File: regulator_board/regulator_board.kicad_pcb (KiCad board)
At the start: 2 copper layers, 68 parts, among them J1 BATT, J10 5VOUT, J11 9VOUT, J12 9VOUT, J13 9VOUT, J2 5VOUT, J3 5VOUT, J4 5VOUT, J5 5VOUT, J6 5VOUT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

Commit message: regulator design preliminary
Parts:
- moved U3 141.8 mm to (122.9, 82.2)
- moved J13 138.7 mm to (163.8, 123.2), turned to 90 degrees
- moved D3 124.8 mm to (112.5, 90.3)
- moved U2 119.9 mm to (117.8, 86.6)
- moved C14 119.8 mm to (122.5, 88.2)
- moved R5 118.7 mm to (131.2, 84.7)
- moved D5 118.0 mm to (107.3, 97.3)
- moved R4 117.2 mm to (140.7, 81.2)
- moved C6 115.2 mm to (125.5, 90.7)
- moved C13 115.1 mm to (129.9, 93.2)
- moved L2 111.3 mm to (100.1, 84.5)
- moved C7 111.2 mm to (116.0, 100.3)
- moved C10 110.5 mm to (136.3, 81.2)
- moved R13 109.8 mm to (135.6, 84.7)
- moved J11 106.4 mm to (148.6, 123.2), turned to 90 degrees
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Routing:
- net +BATT: track 0.00 -> 13.6 mm
- net Net-(JP1-Pad2): track 0.00 -> 6.28 mm
- net /5V_1: track 0.00 -> 4.02 mm
- net GND: track 0.00 -> 1.19 mm, vias 0 -> 11
- added copper zone on F.Cu, net +BATT
- added copper zone on F.Cu, net /5V_1
- added copper zone on B.Cu, net GND
- added copper zone on F.Cu, net GND
- added copper zone on F.Cu, net Net-(C2-Pad1)
- added copper zone on F.Cu, net Net-(C2-Pad2)
- added copper zone on F.Cu, net Net-(C3-Pad2)
- added copper zone on F.Cu, net Net-(F1-Pad1)
- added copper zone on F.Cu, net Net-(F2-Pad2)
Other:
- board outline added: 110.7 x 36.6 mm

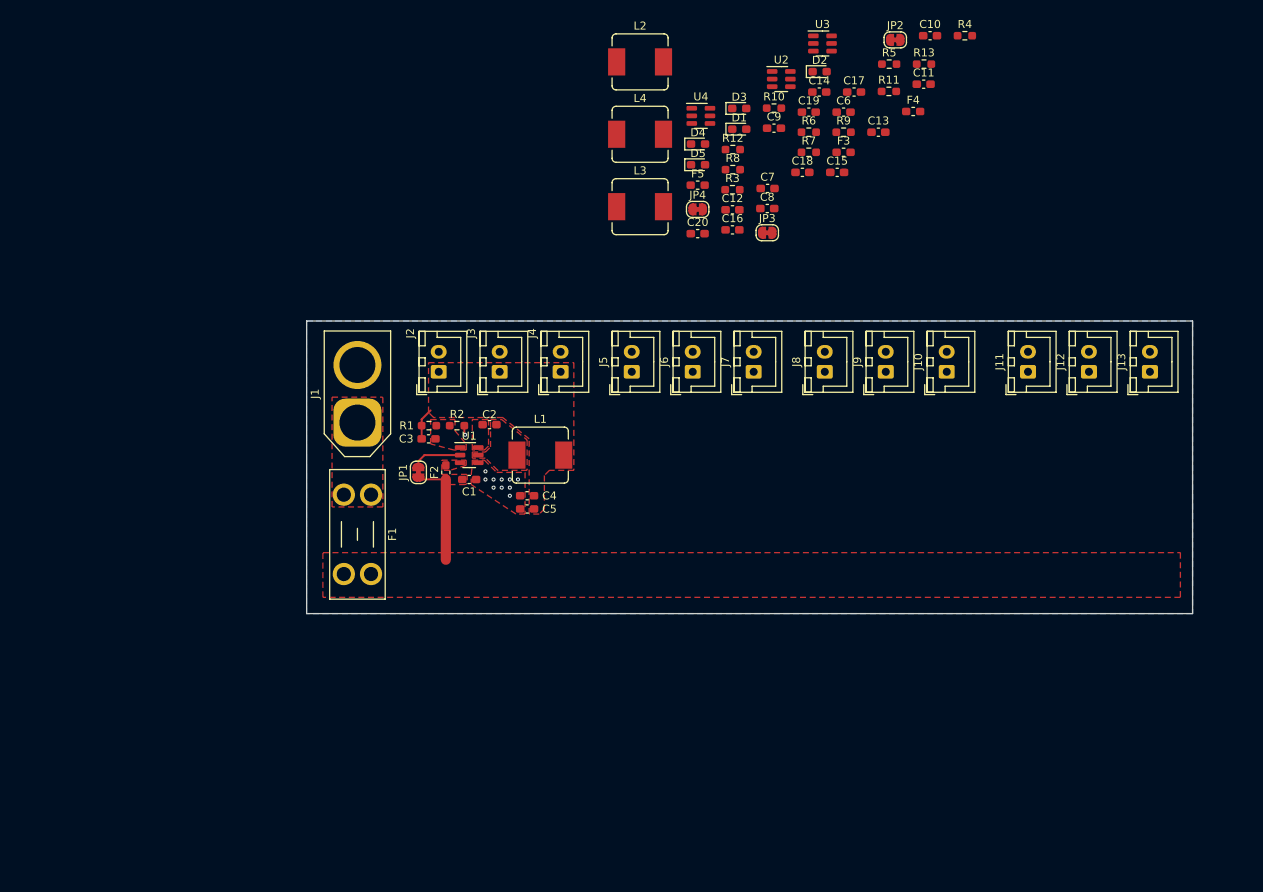
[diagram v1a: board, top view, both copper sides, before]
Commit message: regulator board prelimiary completion
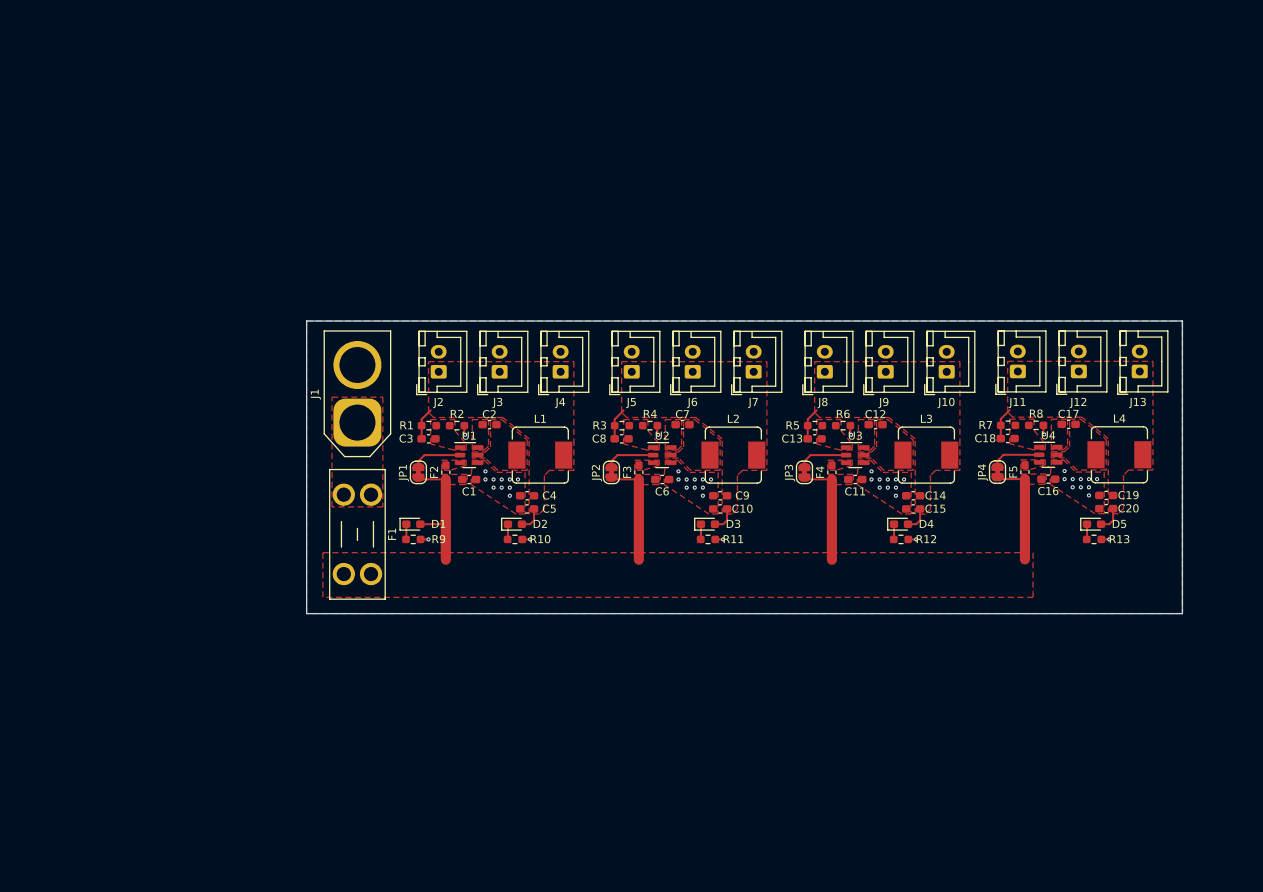
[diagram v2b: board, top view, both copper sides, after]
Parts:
- moved R9 74.1 mm to (71.8, 144.1)
- moved L4 72.1 mm to (160.0, 133.6)
- moved D2 68.2 mm to (84.5, 142.2)
- moved D5 66.9 mm to (156.8, 142.2)
- moved C10 64.7 mm to (110.1, 140.3), turned to 180 degrees
- moved JP2 64.7 mm to (96.5, 135.8), turned to 90 degrees
- moved D1 64.0 mm to (71.8, 142.2)
- moved R13 63.1 mm to (156.8, 144.1)
- moved R10 62.9 mm to (84.5, 144.1)
- moved R4 62.6 mm to (101.3, 129.9)
- moved C20 61.6 mm to (158.4, 140.3), turned to 180 degrees
- moved U4 60.7 mm to (151.1, 133.6)
- moved C19 60.6 mm to (158.4, 138.6), turned to 180 degrees
- moved R11 60.4 mm to (108.6, 144.1)
- moved F5 54.4 mm to (148.2, 135.7), turned to 90 degrees
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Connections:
- C10 pad 1: /5V_3 -> /5V_2
- C13 pad 1: /5V_2 -> /5V_3
- C14 pad 1: /5V_2 -> /5V_3
- C15 pad 1: /5V_2 -> /5V_3
- C8 pad 1: /5V_3 -> /5V_2
- C9 pad 1: /5V_3 -> /5V_2
- J10 pad 1: /5V_2 -> /5V_3
- J5 pad 1: /5V_3 -> /5V_2
- J6 pad 1: /5V_3 -> /5V_2
- J7 pad 1: /5V_3 -> /5V_2
- J8 pad 1: /5V_2 -> /5V_3
- J9 pad 1: /5V_2 -> /5V_3
- L2 pad 2: /5V_3 -> /5V_2
- L3 pad 2: /5V_2 -> /5V_3
- R3 pad 1: /5V_3 -> /5V_2
- R5 pad 1: /5V_2 -> /5V_3
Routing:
- net +BATT: track 13.6 -> 57.6 mm
- net GND: track 1.19 -> 9.71 mm, vias 11 -> 49
- net /9V_1: track 0.00 -> 7.19 mm
- net /5V_2: track 0.00 -> 7.15 mm
- net /5V_3: track 0.00 -> 7.15 mm
- net Net-(JP4-Pad2): track 0.00 -> 6.28 mm
- net Net-(JP2-Pad2): track 0.00 -> 6.28 mm
- net Net-(JP3-Pad2): track 0.00 -> 6.28 mm
- net /5V_1: track 4.02 -> 7.15 mm
- net Net-(D5-Pad1): track 0.00 -> 1.92 mm
- net Net-(D4-Pad1): track 0.00 -> 1.92 mm
- net Net-(D3-Pad1): track 0.00 -> 1.92 mm
- net Net-(D2-Pad1): track 0.00 -> 1.92 mm
- net Net-(D1-Pad1): track 0.00 -> 1.92 mm
- added copper zone on F.Cu, net /5V_2
- added copper zone on F.Cu, net /5V_3
- added copper zone on F.Cu, net /9V_1
- added copper zone on F.Cu, net Net-(C12-Pad1)
- added copper zone on F.Cu, net Net-(C12-Pad2)
- added copper zone on F.Cu, net Net-(C13-Pad2)
- added copper zone on F.Cu, net Net-(C17-Pad1)
- added copper zone on F.Cu, net Net-(C17-Pad2)
- added copper zone on F.Cu, net Net-(C18-Pad2)
- added copper zone on F.Cu, net Net-(C7-Pad1)
- added copper zone on F.Cu, net Net-(C7-Pad2)
- added copper zone on F.Cu, net Net-(C8-Pad2)
- added copper zone on F.Cu, net Net-(F3-Pad2)
- added copper zone on F.Cu, net Net-(F4-Pad2)
- added copper zone on F.Cu, net Net-(F5-Pad2)
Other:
- board size 110.7 x 36.6 mm -> 109.5 x 36.6 mm

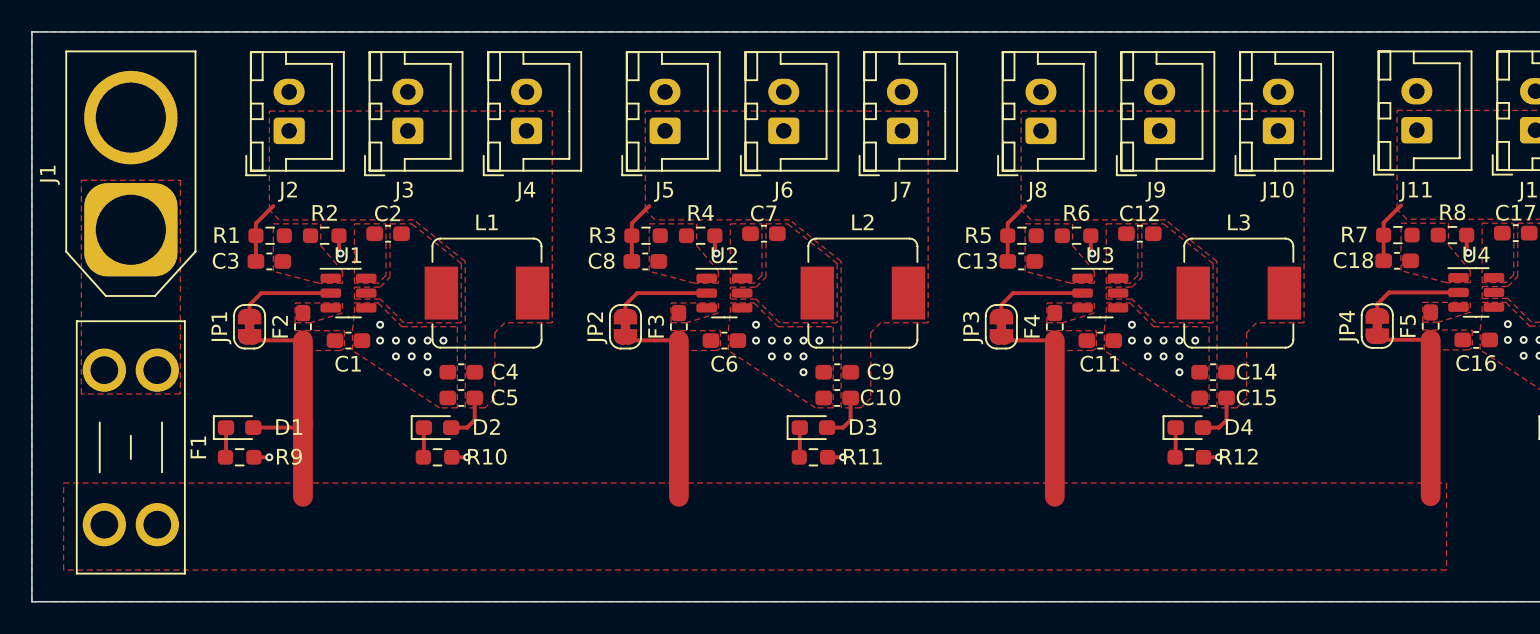
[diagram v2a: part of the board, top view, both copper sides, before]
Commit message: fix regulator xt60 orientation
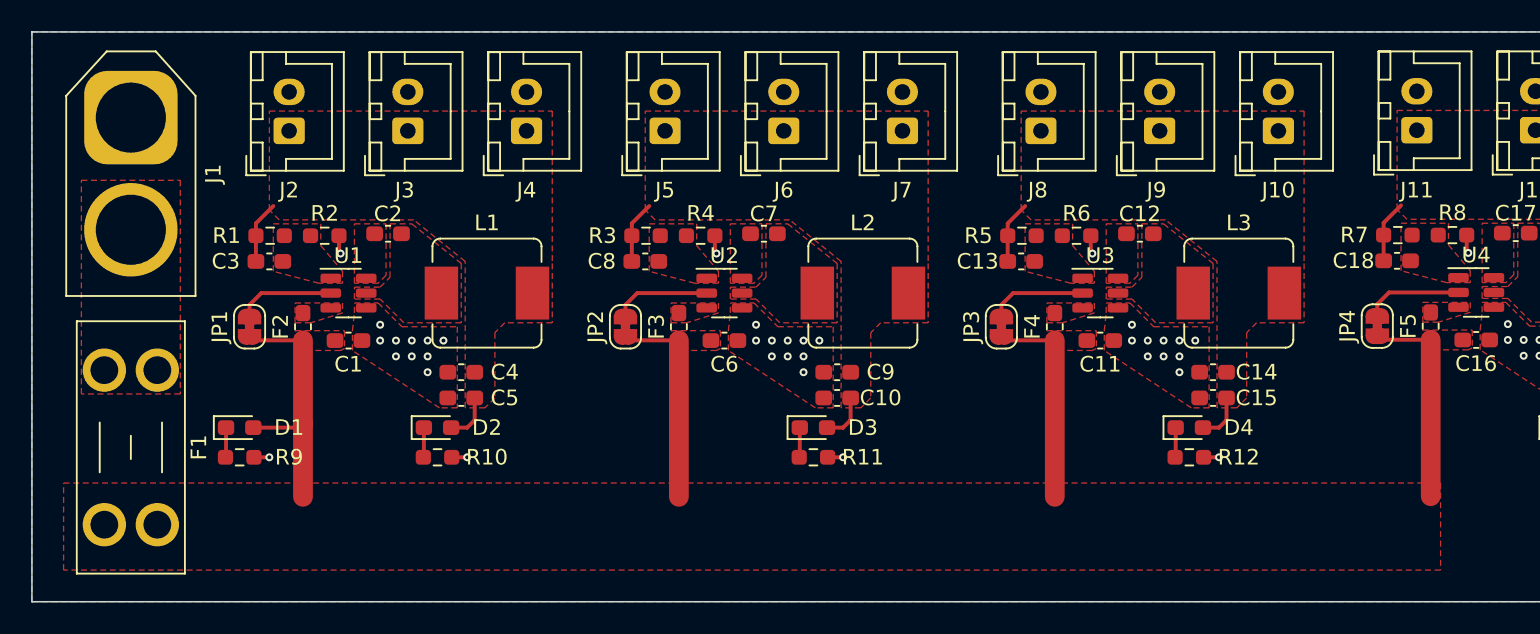
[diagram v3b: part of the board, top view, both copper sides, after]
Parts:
- moved J1 7.20 mm to (64.8, 122.3), turned to -90 degrees
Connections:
- J1 pad 1: Net-(F1-Pad1) -> GND
- J1 pad 2: GND -> Net-(F1-Pad1)

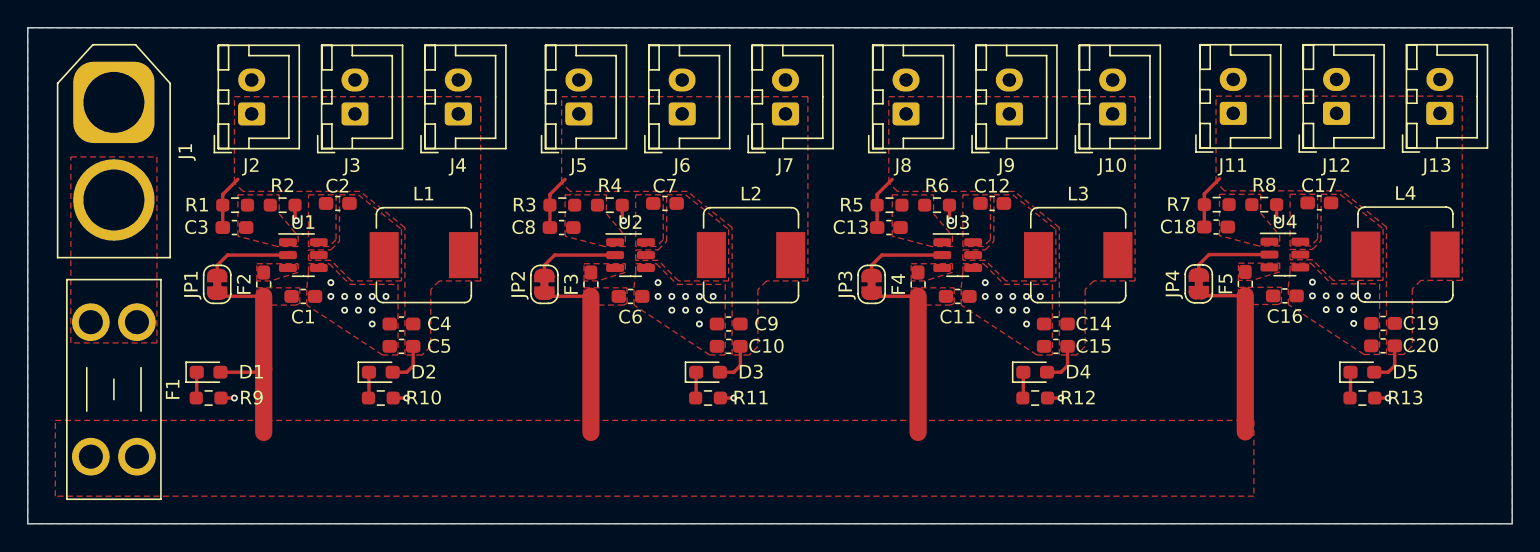
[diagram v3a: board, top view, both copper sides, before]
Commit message: regulator silkscreen and models
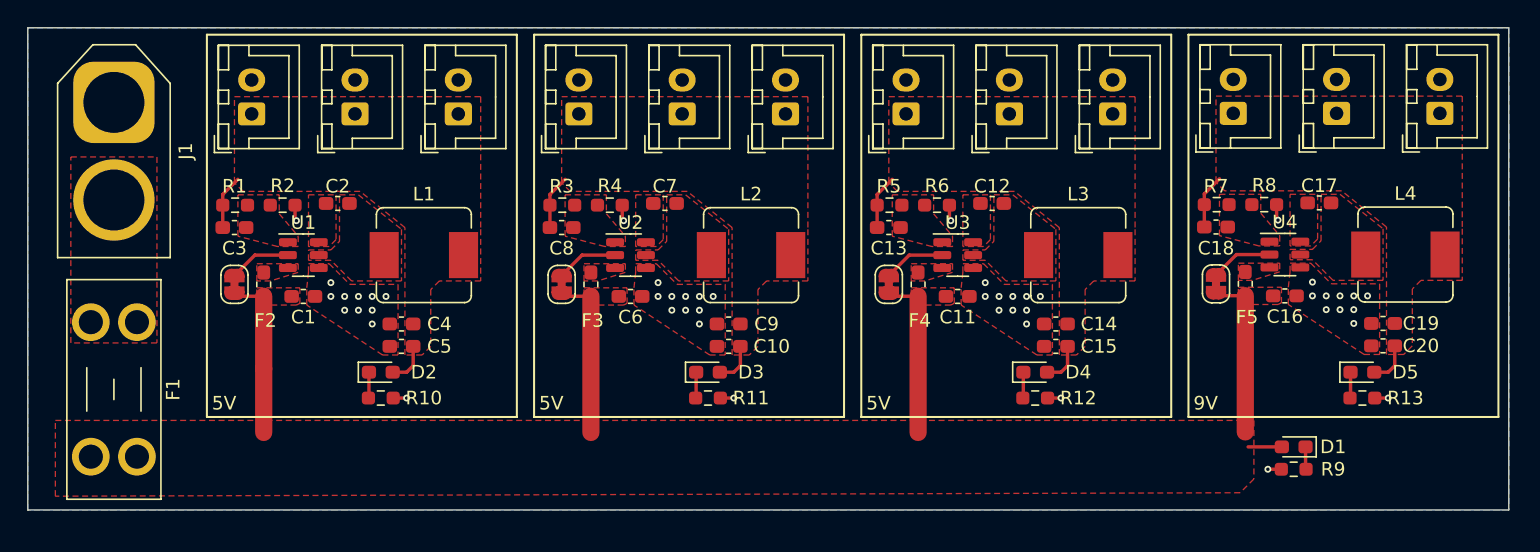
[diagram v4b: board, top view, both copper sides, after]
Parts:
- moved D1 80.2 mm to (151.8, 147.7), turned to 180 degrees
- moved R9 80.2 mm to (151.8, 149.4), turned to 180 degrees
- moved JP2 1.27 mm to (97.8, 135.8)
- moved JP4 1.27 mm to (146.1, 135.7)
- moved JP1 1.27 mm to (73.7, 135.8)
- moved JP3 1.27 mm to (121.9, 135.8)
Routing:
- net +BATT: track 57.6 -> 52.0 mm
- net Net-(JP2-Pad2): track 6.28 -> 4.57 mm
- net Net-(JP4-Pad2): track 6.28 -> 4.57 mm
- net Net-(JP3-Pad2): track 6.28 -> 4.57 mm
- net Net-(JP1-Pad2): track 6.28 -> 4.57 mm
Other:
- board size 109.5 x 36.6 mm -> 109.2 x 35.6 mm
- board text added: "5V"
- board text added: "9V"

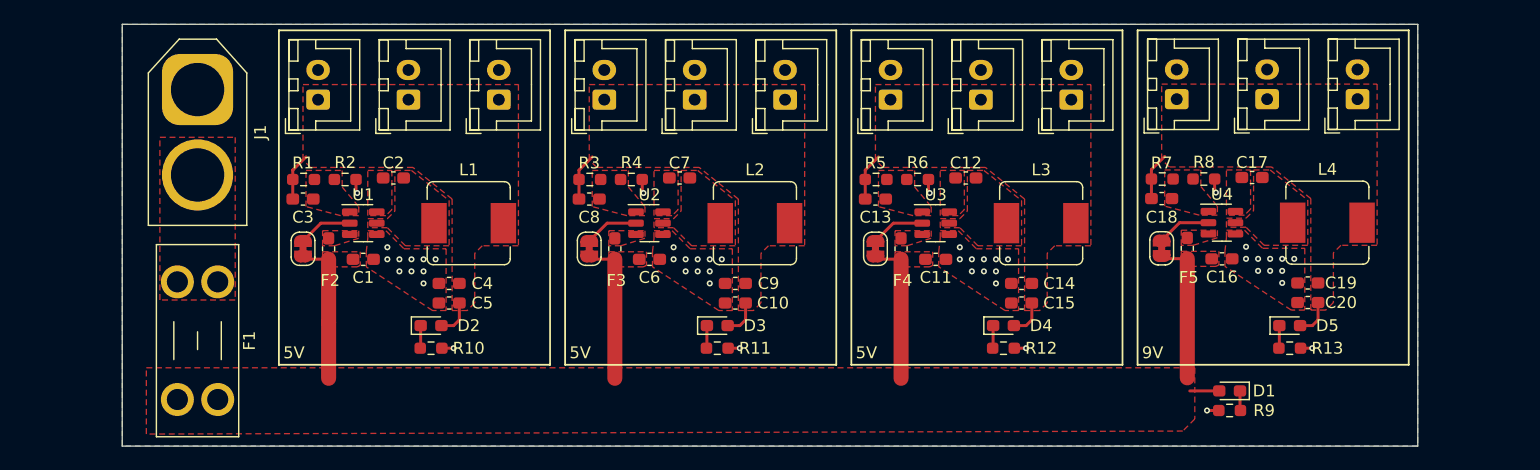
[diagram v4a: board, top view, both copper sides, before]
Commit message: regulator board outline redesign & back graphics
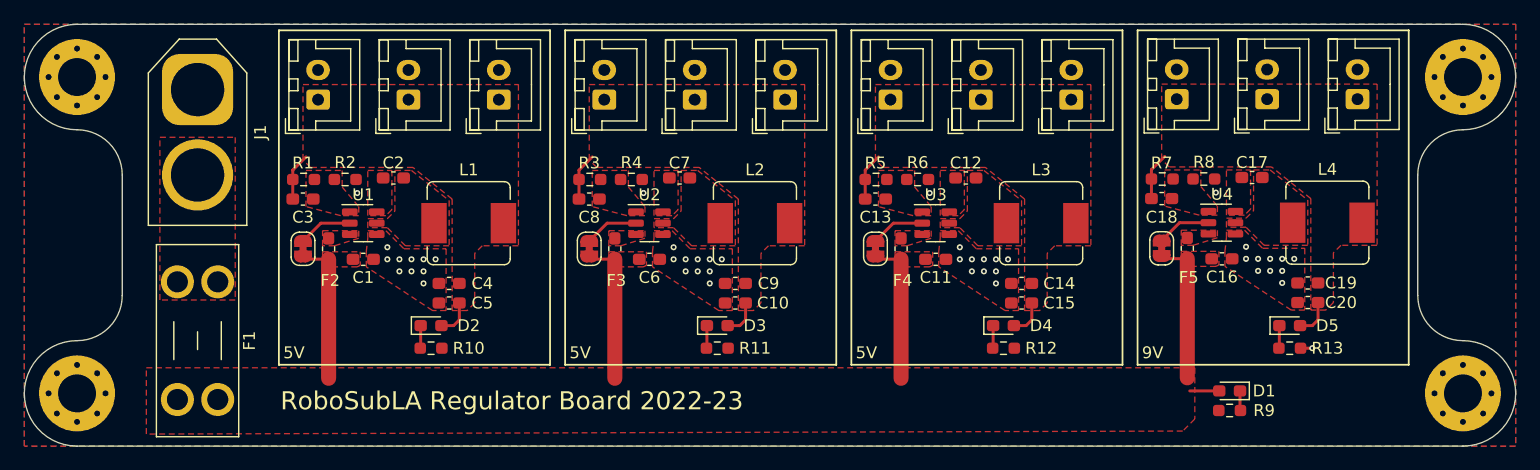
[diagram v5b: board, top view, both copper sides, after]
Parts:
- added H1: MountingHole_Pad, MountingHole:MountingHole_3.2mm_M3_Pad_Via, F.Cu at (54.6, 121.3)
- added H2: MountingHole_Pad, MountingHole:MountingHole_3.2mm_M3_Pad_Via, F.Cu at (54.6, 148.0)
- added H3: MountingHole_Pad, MountingHole:MountingHole_3.2mm_M3_Pad_Via, F.Cu at (171.4, 121.3)
- added H4: MountingHole_Pad, MountingHole:MountingHole_3.2mm_M3_Pad_Via, F.Cu at (171.4, 148.0)
- added LOGO1: Logo_Open_Hardware_Large, Symbol:OSHW-Logo2_9.8x8mm_SilkScreen, B.Cu at (129.5, 147.3)
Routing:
- net GND: track 9.71 -> 0.99 mm, vias 49 -> 45
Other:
- board size 109.2 x 35.6 mm -> 125.7 x 35.6 mm
- board text added: "(it's a small banana)"
- board text added: "Banana For Scale"
- board text added: "Did you ever hear the tragedy of Darth Plagueis The Wise? I thought not. It's not a story the Jedi would tell you. It's a Sith legend. Darth Plagueis was a Dark Lord of the Sith, so powerful and so wise he could use the Force to influence the midichlorians to create life… He had such a knowledge of the dark side that he could even keep the ones he cared about from dying. The dark side of the Forc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"
- board text added: "If you're reading this, either the board is upside down or you are"
- board text added: "RoboSubLA Regulator Board 2022-23"

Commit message: one final graphic
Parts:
- moved LOGO1 3.24 mm to (128.9, 144.1)
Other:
- board text added: "CAUTION: DO NOT EAT"
- board text added: "uwu"
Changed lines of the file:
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@@
   )
   (footprint "Symbol:OSHW-Logo2_9.8x8mm_SilkScreen" (layer "B.Cu")
-    (at 129.54 147.32 180)
+    (at 128.905 144.145 180)
     (descr "Open Source Hardware Symbol")
     (tags "Logo Symbol OSHW")
@@
     (effects (font (size 1.016 1.016) (thickness 0.1524)) (justify mirror))
   )
-  (gr_text "If you're reading this, either the\nboard is upside down or you are" (at 102.235 144.78) (layer "B.SilkS")
+  (gr_text "If you're reading this, either the\nboard is upside down or you are" (at 102.235 147.32) (layer "B.SilkS")
     (effects (font (size 1.524 1.524) (thickness 0.254)) (justify mirror))
   )
@@
     (effects (font (size 1.016 1.016) (thickness 0.1778)) (justify left mirror))
   )
+  (gr_text "uwu" (at 142.24 147.955) (layer "B.SilkS")
+    (effects (font (size 1.016 1.016) (thickness 0.1524)) (justify mirror))
+  )
+  (gr_text "CAUTION: DO NOT EAT" (at 95.885 140.97) (layer "B.SilkS")
+    (effects (font (size 1.524 1.524) (thickness 0.254)) (justify mirror))
+  )
   (gr_text "9V" (at 145.288 144.526) (layer "F.SilkS")
